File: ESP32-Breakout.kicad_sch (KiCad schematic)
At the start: 17 parts, among them J2 USB_C_Receptacle_USB2.0_16P, SW1 USAKRO UK-B0227-G4.3-B-250, SW2 USAKRO UK-B0227-G4.3-B-250, U3 ESP32-S3-WROOM-1U

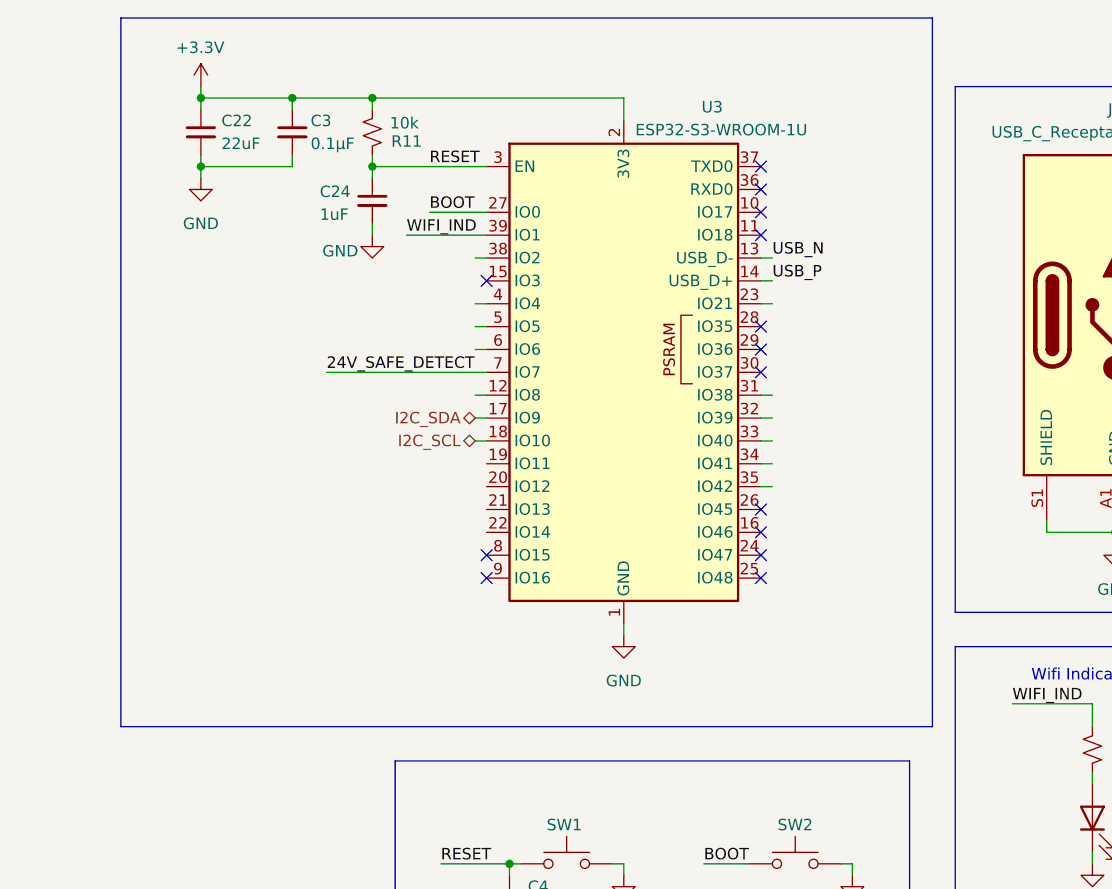
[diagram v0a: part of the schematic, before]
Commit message: Updated most of root-page labels.
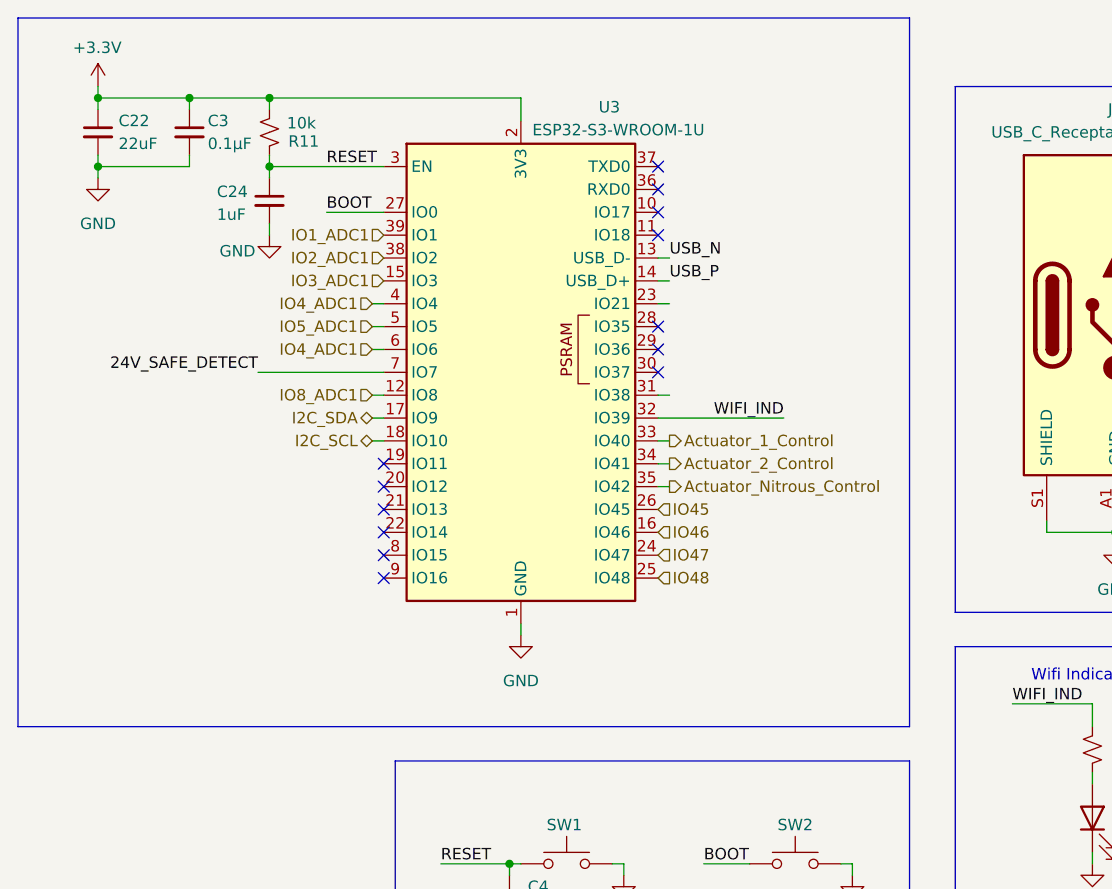
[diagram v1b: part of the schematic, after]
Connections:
- net WIFI_IND: now also U3.32 (IO39); no longer U3.39 (IO1)
- net IO8_ADC1: now reaches U3.12 (IO8)
- net IO3_ADC1: now reaches U3.15 (IO3)
- net IO46: now reaches U3.16 (IO46)
- net IO47: now reaches U3.24 (IO47)
- net IO48: now reaches U3.25 (IO48)
- net IO45: now reaches U3.26 (IO45)
- net Actuator_1_Control: now reaches U3.33 (IO40)
- net Actuator_2_Control: now reaches U3.34 (IO41)
- net Actuator_Nitrous_Control: now reaches U3.35 (IO42)
- net IO2_ADC1: now reaches U3.38 (IO2)
- net IO4_ADC1: now reaches U3.4 (IO4)
- net IO4_ADC1: now also U3.6 (IO6)
- net IO5_ADC1: now reaches U3.5 (IO5)
- new net IO1_ADC1: U3.39 (IO1)
- no-connect marks 16 -> 15
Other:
- moved on the sheet: C22, C24, C3, R11, U3

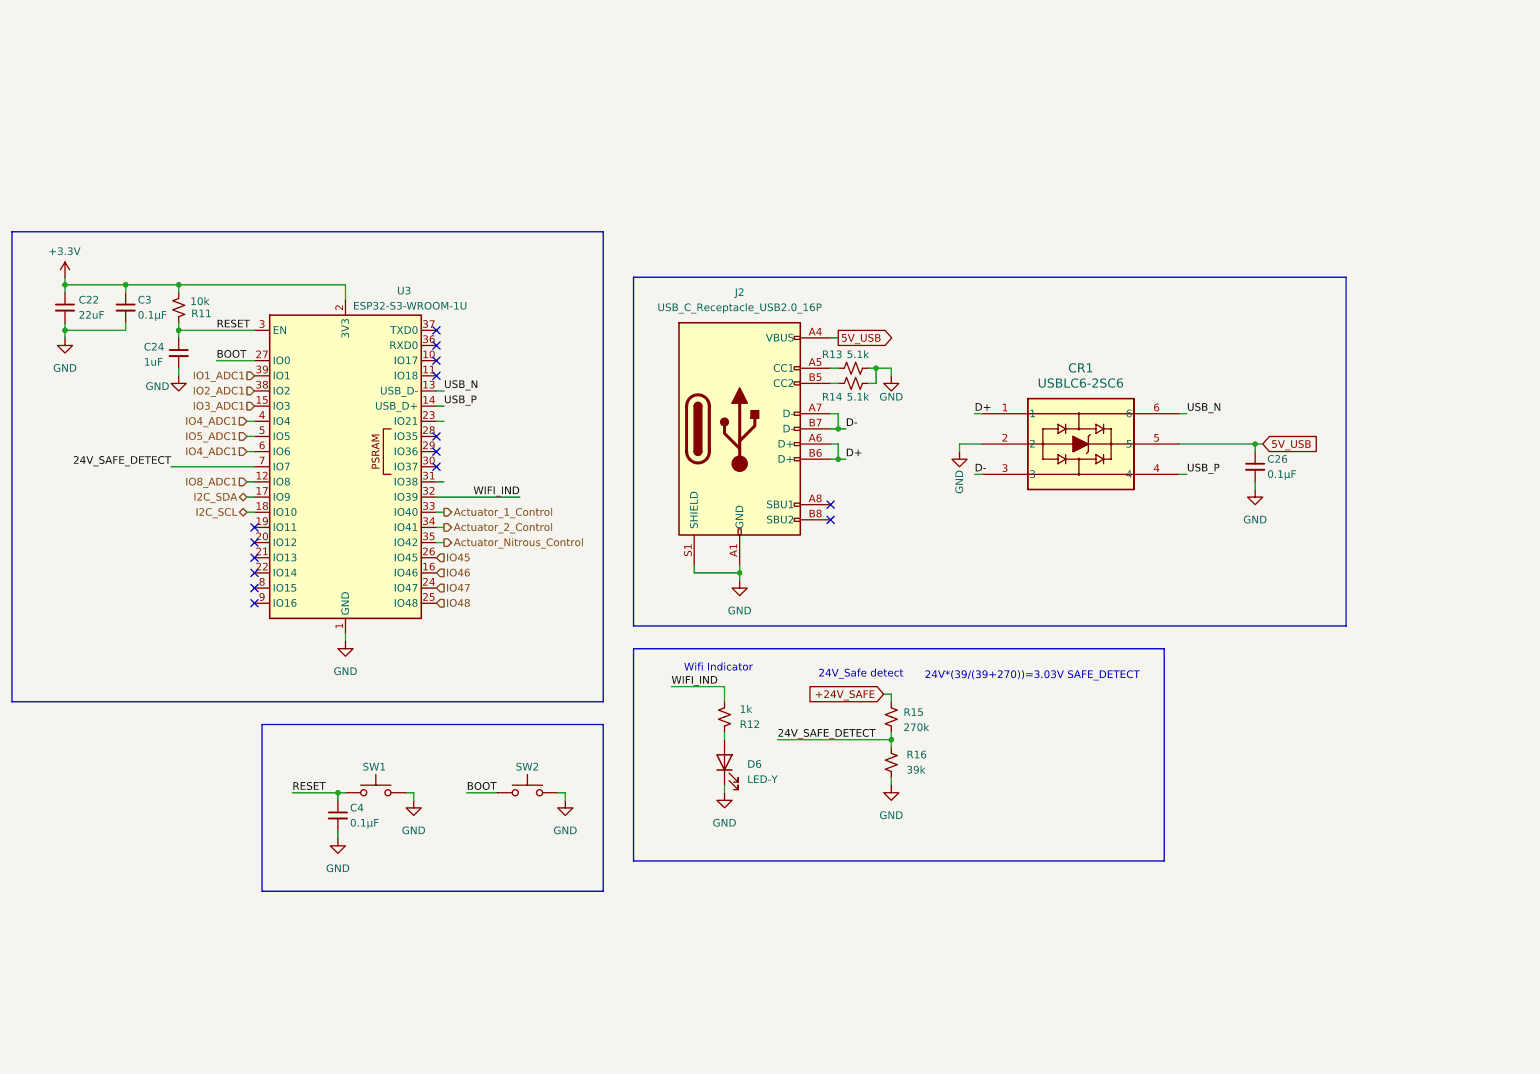
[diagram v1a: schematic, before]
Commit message: Added 24V-12V step-down converter for fans, started switch to devkit.
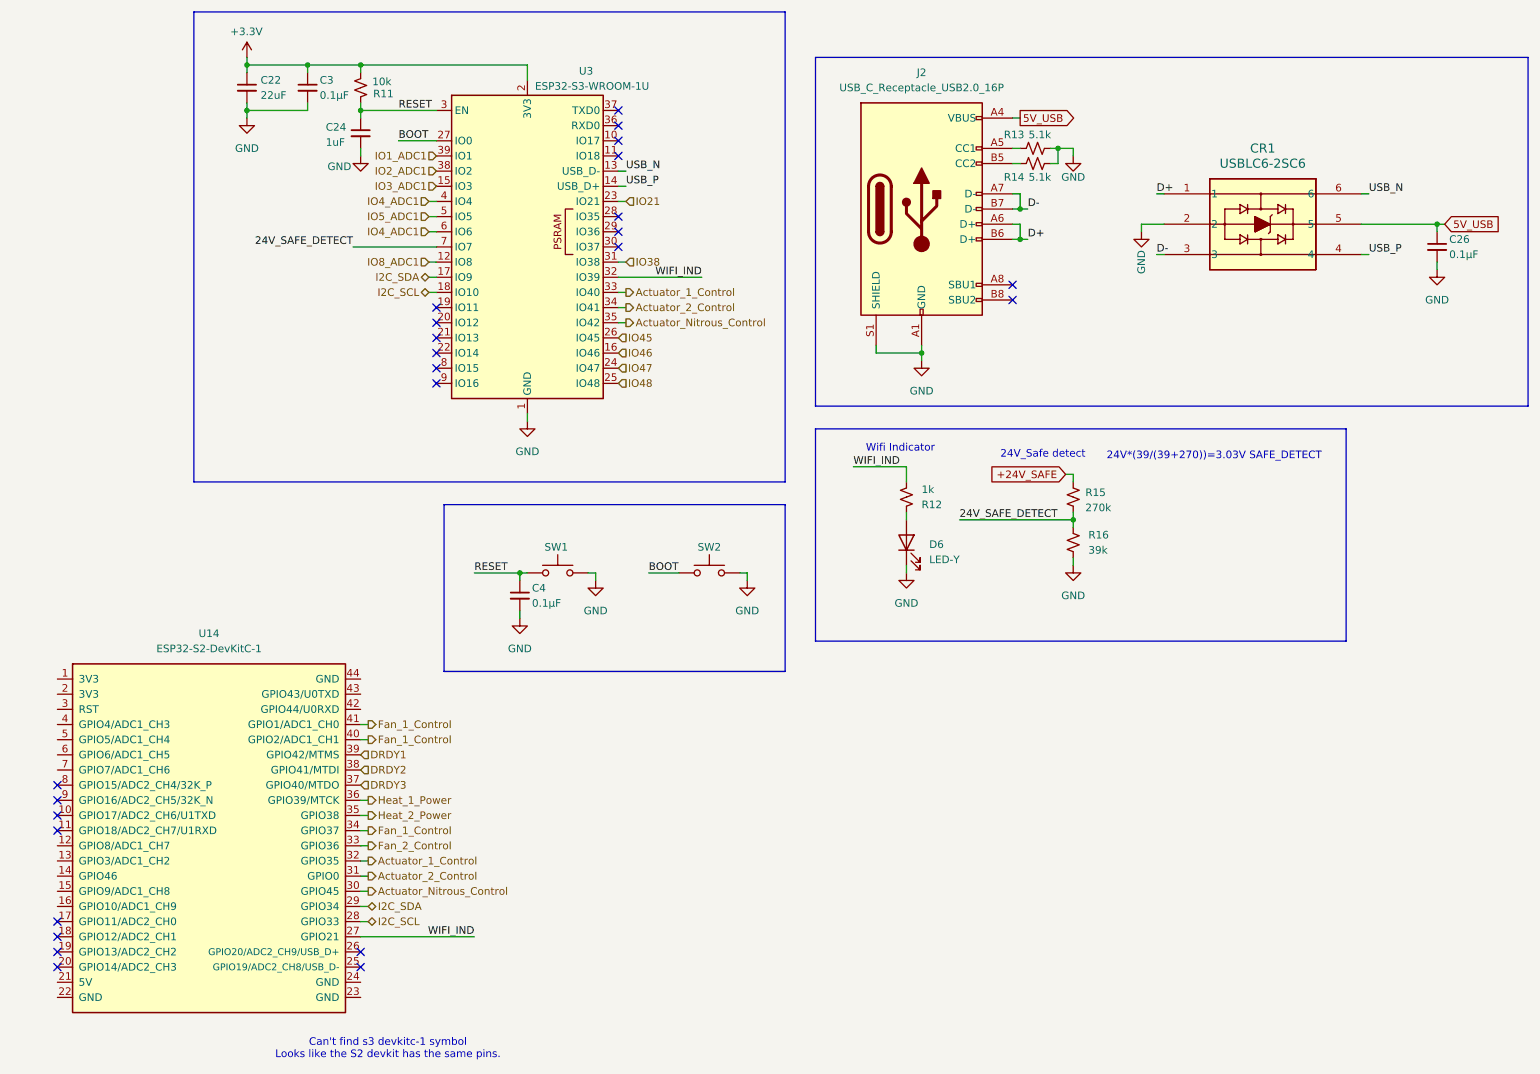
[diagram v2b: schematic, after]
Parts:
- added U14: ESP32-S2-DevKitC-1, PCM_Espressif:ESP32-S2-DevKitC-1, symbol PCM_Espressif:ESP32-S2-DevKitC-1
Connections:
- net Actuator_1_Control: now also U14.32 (GPIO35)
- net Actuator_2_Control: now also U14.31 (GPIO0)
- net Actuator_Nitrous_Control: now also U14.30 (GPIO45)
- net I2C_SCL: now also U14.28 (GPIO33)
- net I2C_SDA: now also U14.29 (GPIO34)
- net WIFI_IND: now also U14.27 (GPIO21)
- net IO21: now reaches U3.23 (IO21)
- net IO38: now reaches U3.31 (IO38)
- new net DRDY1: U14.39 (GPIO42/MTMS)
- new net DRDY2: U14.38 (GPIO41/MTDI)
- new net DRDY3: U14.37 (GPIO40/MTDO)
- new net Fan_1_Control: U14.34 (GPIO37), U14.40 (GPIO2/ADC1_CH1), U14.41 (GPIO1/ADC1_CH0)
- new net Fan_2_Control: U14.33 (GPIO36)
- new net Heat_1_Power: U14.36 (GPIO39/MTCK)
- new net Heat_2_Power: U14.35 (GPIO38)
- no-connect marks 15 -> 25
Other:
- note added: "Can't find s3 devkitc-1 symbol Looks like the S2 devkit has the same pins."
- moved on the sheet: C22, C24, C26, C3, C4, CR1, D6, J2, R11, R12, R13, R14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

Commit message: Updated to 4-pin fans, moved power pages together, deleted old reference.
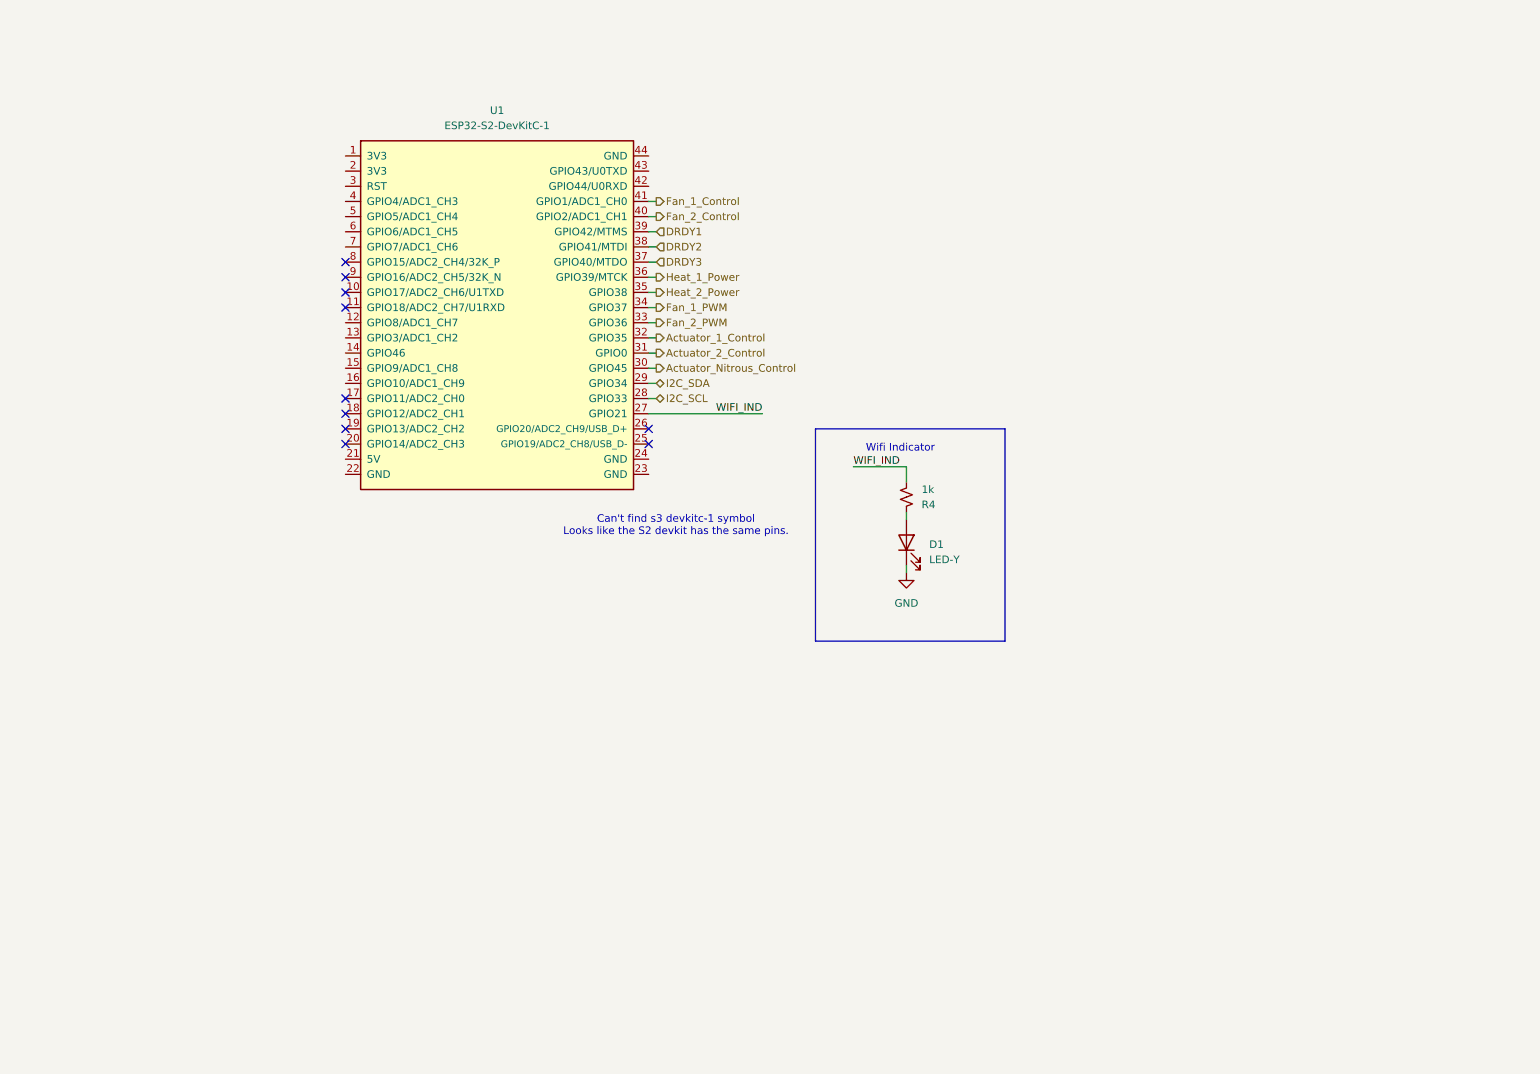
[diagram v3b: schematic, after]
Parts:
- removed C22: 22uF, Capacitor_SMD:C_0805_2012Metric, symbol Device:C_Small
- removed C24: 1uF, Capacitor_SMD:C_0603_1608Metric, symbol Device:C_Small
- removed C26, C3, C4: 0.1μF, Capacitor_SMD:C_0402_1005Metric, symbol Device:C_Small
- removed CR1: USBLC6-2SC6, Package_TO_SOT_SMD:SOT-23-6, symbol USBLC6-2SC6:USBLC6-2SC6
- removed J2: USB_C_Receptacle_USB2.0_16P, Connector_USB:USB_C_Receptacle_G-Switch_GT-USB-7051x, symbol Connector:USB_C_Receptacle_USB2.0_16P
- removed R11: 10k, Resistor_SMD:R_0402_1005Metric, symbol Device:R_Small_US
- removed R13, R14: 5.1k, Resistor_SMD:R_0402_1005Metric, symbol Device:R_Small_US
- removed R15: 270k, Resistor_SMD:R_0402_1005Metric, symbol Device:R_Small_US
- removed R16: 39k, Resistor_SMD:R_0402_1005Metric, symbol Device:R_Small_US
- removed SW1, SW2: USAKRO UK-B0227-G4.3-B-250, Button_Switch_SMD:SW_Tactile_SPST_NO_Straight_CK_PTS636Sx25SMTRLFS, symbol Switch:SW_Push
- removed U3: ESP32-S3-WROOM-1U, RF_Module:ESP32-S3-WROOM-1U, symbol RF_Module:ESP32-S3-WROOM-1
- renumbered D6 to D1, R12 to R4, U14 to U1
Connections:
- net Fan_1_Control: no longer U1.34 (GPIO37), U1.40 (GPIO2/ADC1_CH1)
- net Fan_2_Control: now also U1.40 (GPIO2/ADC1_CH1); no longer U1.33 (GPIO36)
- new net Fan_1_PWM: U1.34 (GPIO37)
- new net Fan_2_PWM: U1.33 (GPIO36)
- no-connect marks 25 -> 10
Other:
- note removed: "24V*(39/(39+270))=3.03V SAFE_DETECT"
- note removed: "24V_Safe detect"
- moved on the sheet: U1

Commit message: Adopted 4-layer setup and organized placement
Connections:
- net 24_Good: now reaches U1.15 (GPIO9/ADC1_CH8)
- net 12_Good: now reaches U1.16 (GPIO10/ADC1_CH9)
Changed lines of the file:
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@@
+	(wire
+		(pts
+			(xy 80.01 77.47) (xy 81.28 77.47)
+		)
+		(stroke
+			(width 0)
+			(type default)
+		)
+	)
+	(wire
+		(pts
+			(xy 80.01 74.93) (xy 81.28 74.93)
+		)
+		(stroke
+			(width 0)
+			(type default)
+		)
+	)
 	(wire
 		(pts
@@
 		)
 	)
+	(hierarchical_label "24_Good"
+		(shape input)
+		(at 80.01 74.93 180)
+		(effects
+			(font
+				(size 1.27 1.27)
+			)
+			(justify right)
+		)
+	)
 	(hierarchical_label "Heat_2_Power"
 		(shape output)
@@
 		)
 	)
+	(hierarchical_label "12_Good"
+		(shape input)
+		(at 80.01 77.47 180)
+		(effects
+			(font
+				(size 1.27 1.27)
+			)
+			(justify right)
+		)
+	)
